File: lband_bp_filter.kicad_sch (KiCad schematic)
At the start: 20 parts

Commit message: More filter work. Add project title to drawings.
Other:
- company: (none) -> Steves Custom Computers
- title: (none) -> PLUTO RF Card Front-End
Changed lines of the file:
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@@
 (kicad_sch (version 20230121) (generator eeschema)
   (paper "A4")
+  (title_block
+    (title "PLUTO RF Card Front-End")
+    (rev " 001")
+    (company "Steves Custom Computers")
+  )
   (junction (at 107.95 90.17) (diameter 0) (color 0 0 0 0)
   )

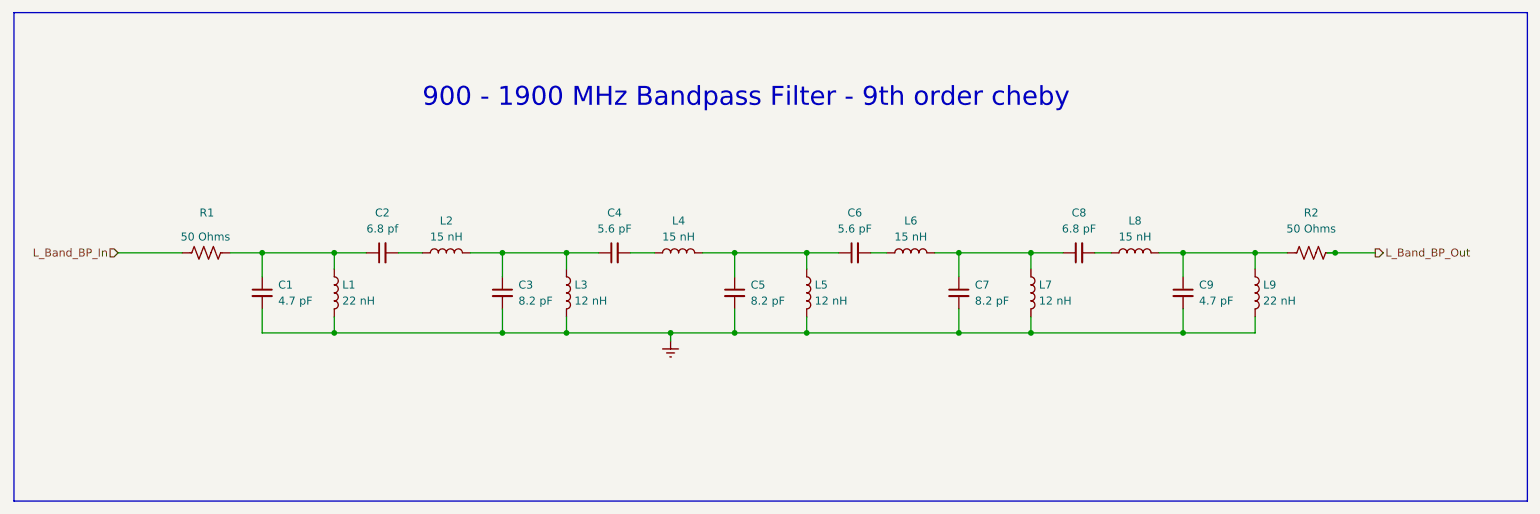
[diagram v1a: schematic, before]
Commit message: Major restructure. Add power/control busses.
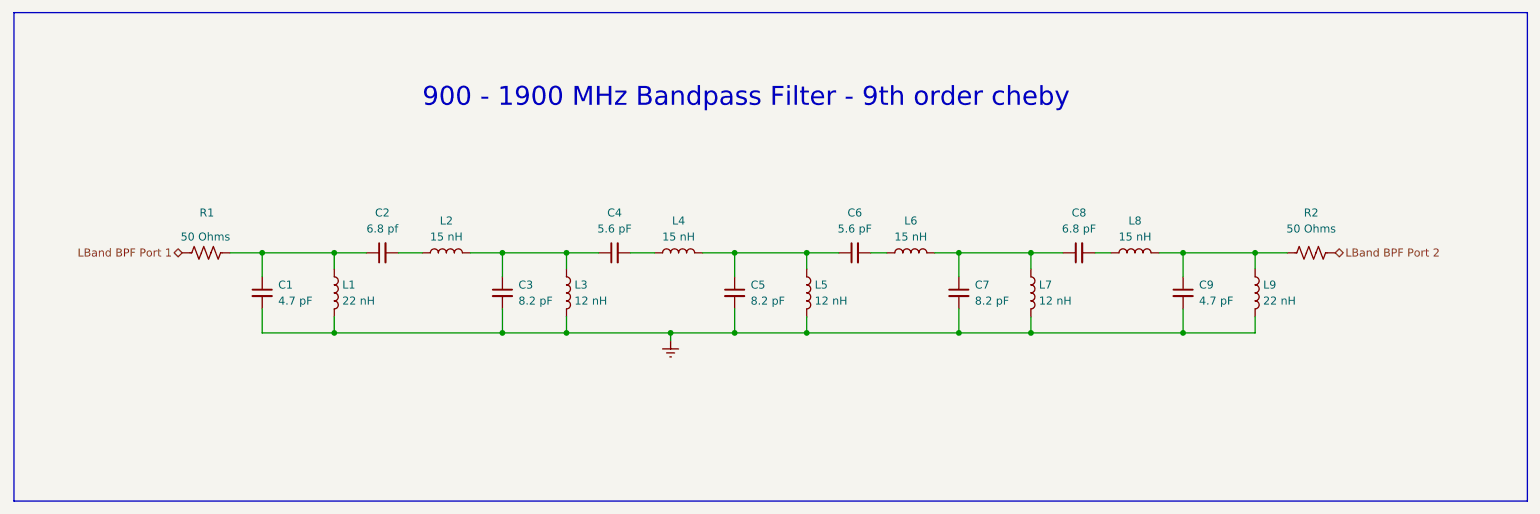
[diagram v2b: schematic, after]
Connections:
- net L_Band_BP_In renamed LBand BPF Port 1
- net L_Band_BP_Out renamed LBand BPF Port 2
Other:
- title: PLUTO RF Card Front-End -> PLUTO RF Front-End Card
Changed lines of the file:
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@@
   (paper "A4")
   (title_block
-    (title "PLUTO RF Card Front-End")
+    (title "PLUTO RF Front-End Card")
     (rev " 001")
     (company "Steves Custom Computers")
@@
   (junction (at 107.95 77.47) (diameter 0) (color 0 0 0 0)
   )
-  (junction (at 240.03 77.47) (diameter 0) (color 0 0 0 0)
-  )
   (junction (at 180.34 90.17) (diameter 0) (color 0 0 0 0)
   )
@@
     (stroke (width 0) (type default))
   )
-  (wire (pts (xy 240.03 77.47) (xy 246.38 77.47))
-    (stroke (width 0) (type default))
-  )
   (wire (pts (xy 215.9 77.47) (xy 227.33 77.47))
     (stroke (width 0) (type default))
@@
     (stroke (width 0) (type default))
   )
-  (wire (pts (xy 46.99 77.47) (xy 57.15 77.47))
-    (stroke (width 0) (type default))
-  )
   (wire (pts (xy 144.78 86.36) (xy 144.78 90.17))
     (stroke (width 0) (type default))
@@
   )
   (wire (pts (xy 212.09 77.47) (xy 215.9 77.47))
-    (stroke (width 0) (type default))
-  )
-  (wire (pts (xy 238.76 77.47) (xy 240.03 77.47))
     (stroke (width 0) (type default))
   )
@@
     (effects (font (size 3 3)) (justify left bottom))
   )
-  (hierarchical_label "L_Band_BP_In" (shape input) (at 46.99 77.47 180) (fields_autoplaced)
+  (hierarchical_label "LBand BPF Port 1" (shape bidirectional) (at 57.15 77.47 180) (fields_autoplaced)
     (effects (font (size 1.27 1.27)) (justify right))
   )
-  (hierarchical_label "L_Band_BP_Out" (shape output) (at 246.38 77.47 0) (fields_autoplaced)
+  (hierarchical_label "LBand BPF Port 2" (shape bidirectional) (at 240.03 77.47 0) (fields_autoplaced)
     (effects (font (size 1.27 1.27)) (justify left))
   )
